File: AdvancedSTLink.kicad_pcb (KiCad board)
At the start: 4 copper layers, 49.9 x 32 mm, 114 parts, among them J1 USB_C_Receptacle, J2 Conn_02x03_Odd_Even, J3 Conn_01x06, J4 Conn_02x03_Odd_Even, Q1 S8050, SW1 SW_SPDT, U1 STM32F205RETx, U2 XC6206P332MR, U3 USBLC6-2P6, U4 MP2359, U5 USBLC6-2P6, U6 USBLC6-2P6, Y1 X322512MSB4SI

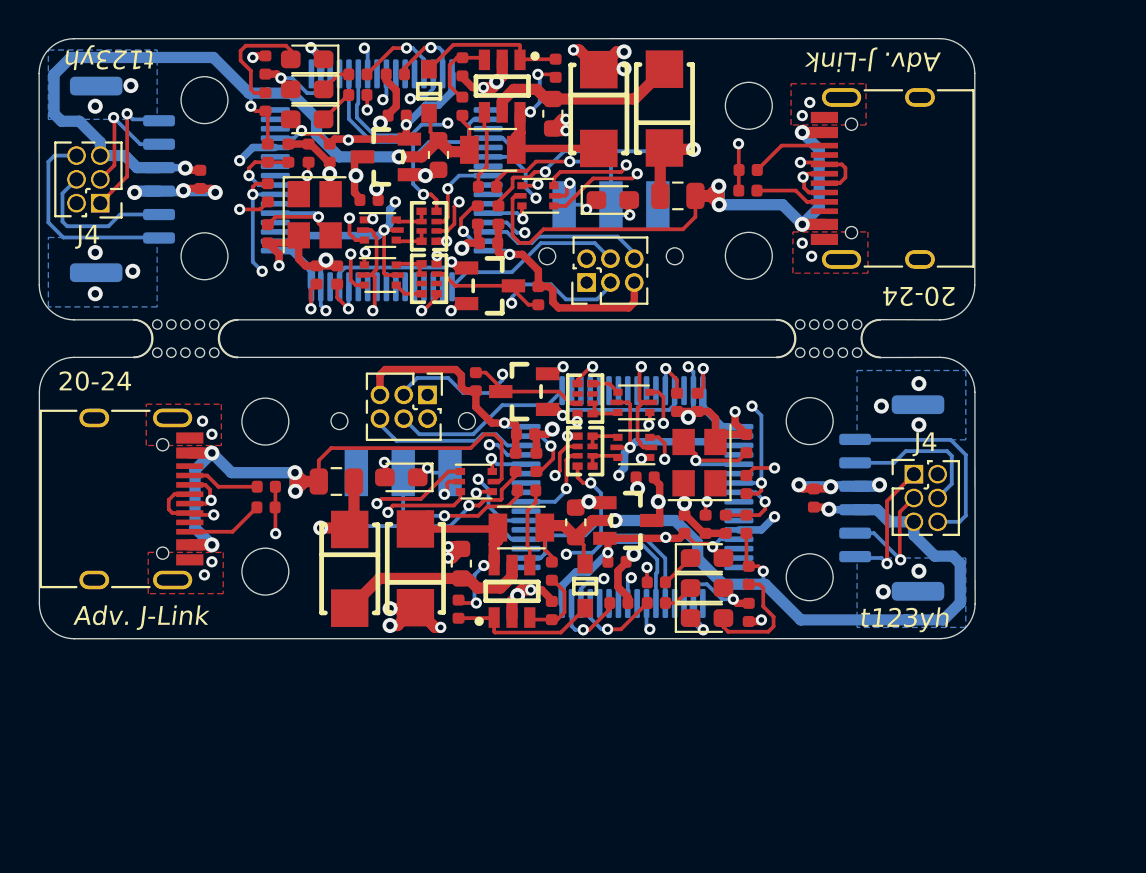
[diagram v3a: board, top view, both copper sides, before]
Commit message: Change DCDC design.
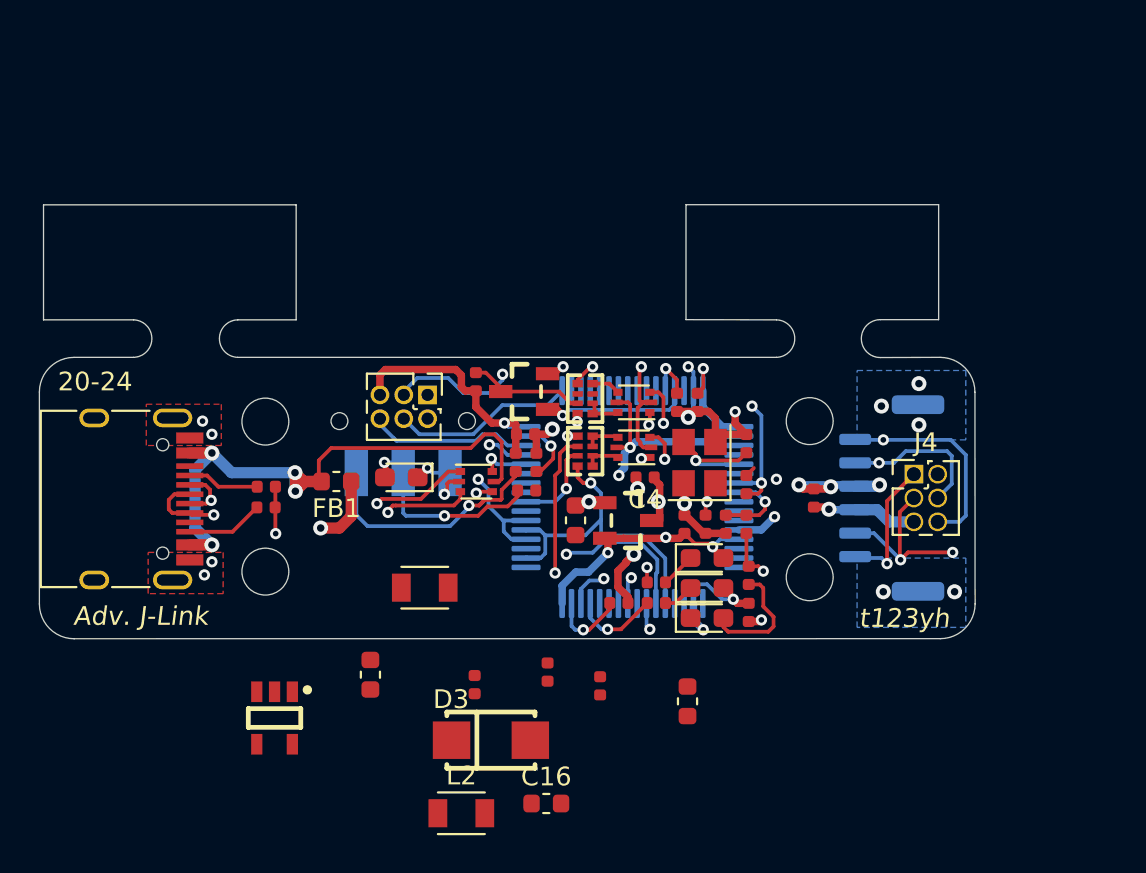
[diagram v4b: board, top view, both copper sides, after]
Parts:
- removed the C1 at (176.6, 86.1)
- removed the C10 at (177.7, 86.1)
- removed the C11 at (174.3, 81.4)
- removed the C12 at (183.5, 86.2)
- removed the C13 at (181.2, 81.9)
- removed the C14 at (185.6, 89.4)
- removed the C15 at (170.8, 87.5)
- removed the C2 at (174.4, 90.4)
- removed the C3 at (174.4, 88.2)
- removed the C4 at (179.8, 88.6)
- removed the C5 at (181.3, 84.1)
- removed the C6 at (189.6, 84.0)
- removed the C7 at (189.7, 81.6)
- removed the C7 at (184.6, 110.4)
- removed the C8 at (177.0, 92.6)
- removed the C9 at (186.2, 90.9)
- removed the D1 at (176.5, 82.7)
- removed the D2 at (176.5, 84.3)
- removed the D3 at (192.0, 83.8)
- removed the D3 at (182.2, 108.2)
- removed D4 (x2): 1N4148W, lc:SOD-323
- removed the D5 at (176.5, 81.1)
- removed the D6 at (192.8, 88.6)
- removed D7 (x2): SS34, lc:SMA(DO-214AC)_S1
- removed the FB1 at (196.2, 88.4)
- removed the H1 at (171.0, 91.6)
- removed the H2 at (171.0, 83.3)
- removed the H3 at (200.0, 91.6)
- removed the H4 at (200.0, 83.6)
- removed the J1 at (208.1, 87.5)
- removed the J2 at (191.4, 93.0)
- removed the J3 at (166.6, 87.5)
- removed the J4 at (165.4, 88.8)
- removed the L1 at (186.4, 85.9)
- removed the Q1 at (186.2, 93.2)
- removed the R1 at (186.1, 87.9)
- removed the R14 at (184.8, 83.6)
- removed the R15 at (184.8, 81.5)
- removed the R16 at (174.3, 83.4)
- removed the R17 at (178.1, 92.6)
- removed the R2 at (175.5, 86.1)
- removed the R3 at (174.4, 86.1)
- removed the R4 at (200.0, 88.1)
- removed the R5 at (200.0, 87.0)
- removed the R6 at (188.8, 93.7)
- removed the R7 at (179.2, 81.9)
- removed the R8 at (179.2, 83.0)
- removed the R9 at (186.7, 89.4)
- removed the RN1 at (183.0, 90.0)
- removed the RN2 at (183.0, 92.8)
- removed the SW1 at (192.7, 91.6)
- removed the U1 at (180.5, 87.6)
- removed the U2 at (180.7, 86.3)
- removed the U3 at (188.8, 88.4)
- removed the U4 at (186.9, 82.5)
- removed the U4 at (187.4, 109.5)
- removed the U5 at (180.4, 92.6)
- removed the U6 at (180.4, 90.2)
- removed the Y1 at (176.9, 89.4)
- removed mouse-bite-3mm-slot (x2): VAL**, mouse_bite:mouse-bite-3mm-slot
- added C16: 4.7uF, Capacitor_SMD:C_0603_1608Metric, F.Cu at (189.2, 120.8)
- added C7: 33pF, Capacitor_SMD:C_0402_1005Metric, F.Cu at (185.4, 114.5)
- added D3: SS34, lc:SMA(DO-214AC)_S1, F.Cu at (186.3, 117.4)
- added L2: DFE252012P-2R2M, Inductor_SMD:L_TDK_NLV25_2.5x2.0mm, F.Cu at (184.7, 121.3)
- added U4: GM9038, lc:SOT-23-5, F.Cu at (174.7, 116.2)
- C4: value 2.2uF -> 1uF
- C5: value 2.2uF -> 4.7uF; footprint Capacitor_SMD:C_0402_1005Metric -> Capacitor_SMD:C_0603_1608Metric
- FB1: footprint Inductor_SMD:L_0805_2012Metric -> Inductor_SMD:L_0603_1608Metric
- L1: value DFE252010P-4R7M -> DFE252012P-2R2M
- R14: value 120k -> 68k
- R15: value 39k -> 15k
- R16: value 1.8k -> 1.5k
- R9: value 2.2k -> 1.5k
- moved C12 11.2 mm to (196.8, 115.3)
- moved C6 7.65 mm to (179.8, 113.9)
- moved L1 6.07 mm to (182.8, 109.3)
- moved R14 5.38 mm to (189.3, 113.8)
- moved R15 4.77 mm to (192.1, 114.5)
- moved C5 3.13 mm to (190.8, 105.7), turned to 90 degrees
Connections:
- C12 pad 1: V_OUT_3.3 -> Net-(C12-Pad1)
- L1 pad 2: V_OUT_3.3 -> Net-(C12-Pad1)
- R14 pad 2: V_OUT_3.3 -> Net-(C12-Pad1)
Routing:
- net GND: track 122.3 -> 47.8 mm, vias 72 -> 29
- net +3V3: track 138.1 -> 68.6 mm, vias 16 -> 8
- net V_OUT_3.3: track 89.4 -> 38.1 mm, vias 6 -> 2
- net T_SWCLK_O: track 59.5 -> 21.6 mm
- net T_SWDIO_O: track 59.0 -> 25.4 mm
- net VBUS: track 64.2 -> 31.6 mm, vias 4 -> 2
- net Net-(FB1-Pad2): track 63.7 -> 31.9 mm, vias 8 -> 4
- net STM_NRST: track 55.7 -> 27.9 mm, vias 6 -> 3
- net Net-(L1-Pad1): track 22.8 -> 0.00 mm, vias 4 -> 0
- net T_SWO_O: track 47.8 -> 25.6 mm, vias 4 -> 2
- net TDO: track 43.9 -> 21.9 mm, vias 4 -> 2
- net Net-(C6-Pad1): track 21.0 -> 0.00 mm
- net USB_IN_DP: track 36.5 -> 18.3 mm, vias 4 -> 2
- net Net-(C7-Pad1): track 17.5 -> 0.00 mm
- net TCK1: track 34.8 -> 17.4 mm, vias 2 -> 1
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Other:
- board size 49.9 x 32 mm -> 49.9 x 23.1 mm

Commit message: Layout.
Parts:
- added C17: 10uF, Capacitor_SMD:C_0603_1608Metric, F.Cu at (188.6, 104.8)
- added H5: MouseBite, mouse_bite:mouse-bite-3mm-slot, F.Cu at (170.1, 96.0)
- added H6: MouseBite, mouse_bite:mouse-bite-3mm-slot, F.Cu at (204.3, 96.0)
- C12: value 22uF -> 10uF
- moved C16 22.9 mm to (209.1, 109.4)
- moved L2 14.2 mm to (188.1, 107.5), turned to 270 degrees
- moved D3 12.1 mm to (178.6, 108.1), turned to 270 degrees
- moved U4 11.4 mm to (182.3, 107.7), turned to 0 degrees
- moved C12 10.2 mm to (187.9, 110.3), turned to 0 degrees
- moved R15 9.04 mm to (183.9, 110.7), turned to 90 degrees
- moved R1 5.78 mm to (182.6, 105.6), turned to 0 degrees
- moved R14 4.68 mm to (185.4, 111.2), turned to 0 degrees
- moved C7 4.35 mm to (185.4, 110.1), turned to 180 degrees
- moved C6 3.95 mm to (181.8, 110.5), turned to 0 degrees
- moved L1 3.36 mm to (185.6, 107.5), turned to 270 degrees
- moved C13 2.51 mm to (190.6, 110.3), turned to 0 degrees
- moved FB1 0.22 mm to (178.0, 103.4)
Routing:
- net GND: track 47.8 -> 57.6 mm, vias 29 -> 42
- net Net-(C12-Pad1): track 0.00 -> 9.14 mm
- net Net-(C6-Pad1): track 0.00 -> 7.53 mm
- net Net-(C7-Pad2): track 0.00 -> 5.81 mm
- net V_OUT_3.3: track 38.1 -> 42.9 mm, vias 2 -> 6
- net Net-(R1-Pad1): track 0.00 -> 4.38 mm
- net Net-(D6-Pad2): track 12.6 -> 8.67 mm
- net TMS2: track 16.4 -> 13.0 mm
- net Net-(FB1-Pad2): track 31.9 -> 28.6 mm
- net VBUS: track 31.6 -> 34.2 mm, vias 2 -> 3
- net Net-(L1-Pad1): track 0.00 -> 2.53 mm
- net +3V3: track 68.6 -> 69.8 mm
- net Net-(C13-Pad2): track 4.29 -> 3.36 mm
- net TMS1: track 15.4 -> 14.7 mm
- net Net-(R9-Pad2): track 13.1 -> 12.6 mm
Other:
- board text removed: "t123yh"

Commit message: Layout optimizations.
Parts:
- added C18: 100nF, Capacitor_SMD:C_0402_1005Metric, F.Cu at (190.9, 109.5)
- D5: value LED_Blue -> LED_Green
- R16: value 1.5k -> 2.2k
- moved C13 0.37 mm to (190.9, 110.6)
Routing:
- net GND: track 57.6 -> 60.5 mm, vias 42 -> 43
- net +3V3: track 69.8 -> 70.8 mm

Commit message: Fixes.
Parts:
- FB1: footprint Inductor_SMD:L_0603_1608Metric -> Inductor_SMD:L_0805_2012Metric
- moved C17 0.08 mm to (188.6, 104.7)
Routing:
- net VBUS: track 34.2 -> 35.1 mm

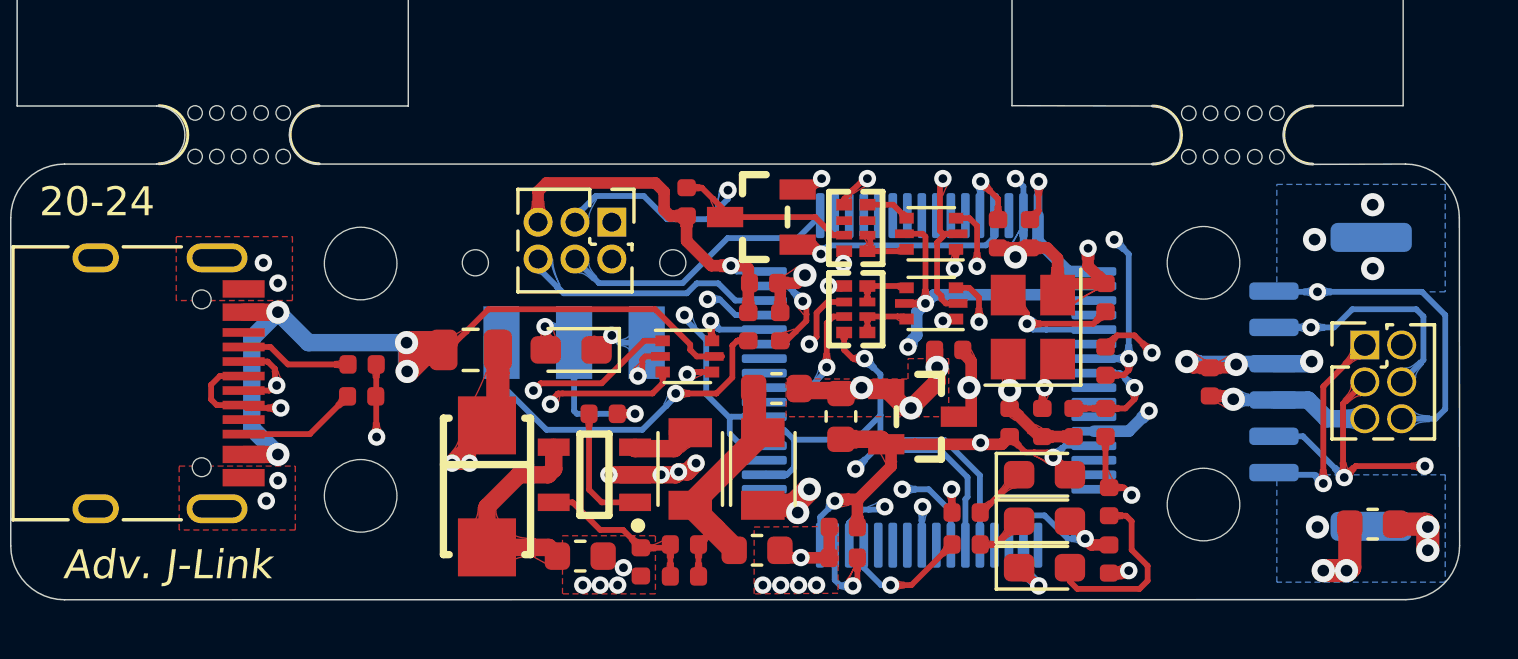
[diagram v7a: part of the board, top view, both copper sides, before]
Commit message: Move ESD.
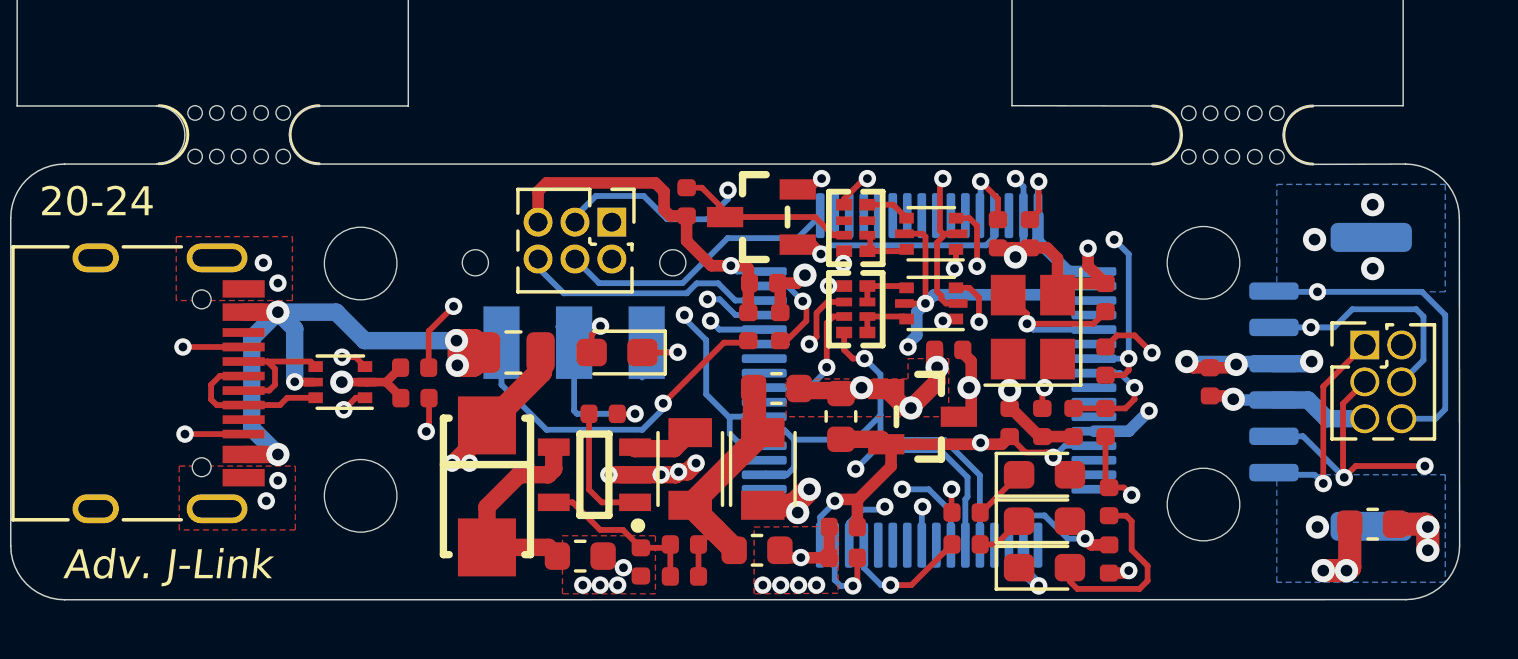
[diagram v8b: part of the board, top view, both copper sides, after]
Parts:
- moved U3 12.0 mm to (173.6, 104.5), turned to 180 degrees
- moved R5 1.84 mm to (176.1, 105.1), turned to 0 degrees
- moved R4 1.81 mm to (176.1, 104.0), turned to 0 degrees
- moved D6 1.58 mm to (183.1, 103.5)
- moved FB1 1.48 mm to (179.5, 103.5)
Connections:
- U3 pad 1: USB_IN_DN -> USB_DP
- U3 pad 3: USB_IN_DP -> USB_DN
- U3 pad 4: USB_DP -> USB_IN_DN
- U3 pad 6: USB_DN -> USB_IN_DP
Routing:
- net Net-(J1-PadA5): track 3.84 -> 22.1 mm, vias 0 -> 2
- net Net-(J1-PadB5): track 4.12 -> 20.8 mm, vias 0 -> 2
- net USB_DN: track 2.68 -> 18.0 mm, vias 1 -> 2
- net USB_IN_DP: track 18.3 -> 5.53 mm, vias 2 -> 0
- net USB_IN_DN: track 17.0 -> 4.62 mm, vias 2 -> 0
- net USB_DP: track 6.85 -> 19.2 mm
- net Net-(FB1-Pad2): track 28.6 -> 23.2 mm, vias 4 -> 5
- net VBUS: track 35.1 -> 36.2 mm
- net GND: track 60.5 -> 59.6 mm, vias 43 -> 42
- net Net-(R9-Pad2): track 12.6 -> 12.0 mm
- added copper zone on F.Cu, net Net-(FB1-Pad2)
